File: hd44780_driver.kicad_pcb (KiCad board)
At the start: 2 copper layers, 25 parts, among them J2 BL, J3 Conn_01x08, Q1 2N7002, U1 PCA9555APW

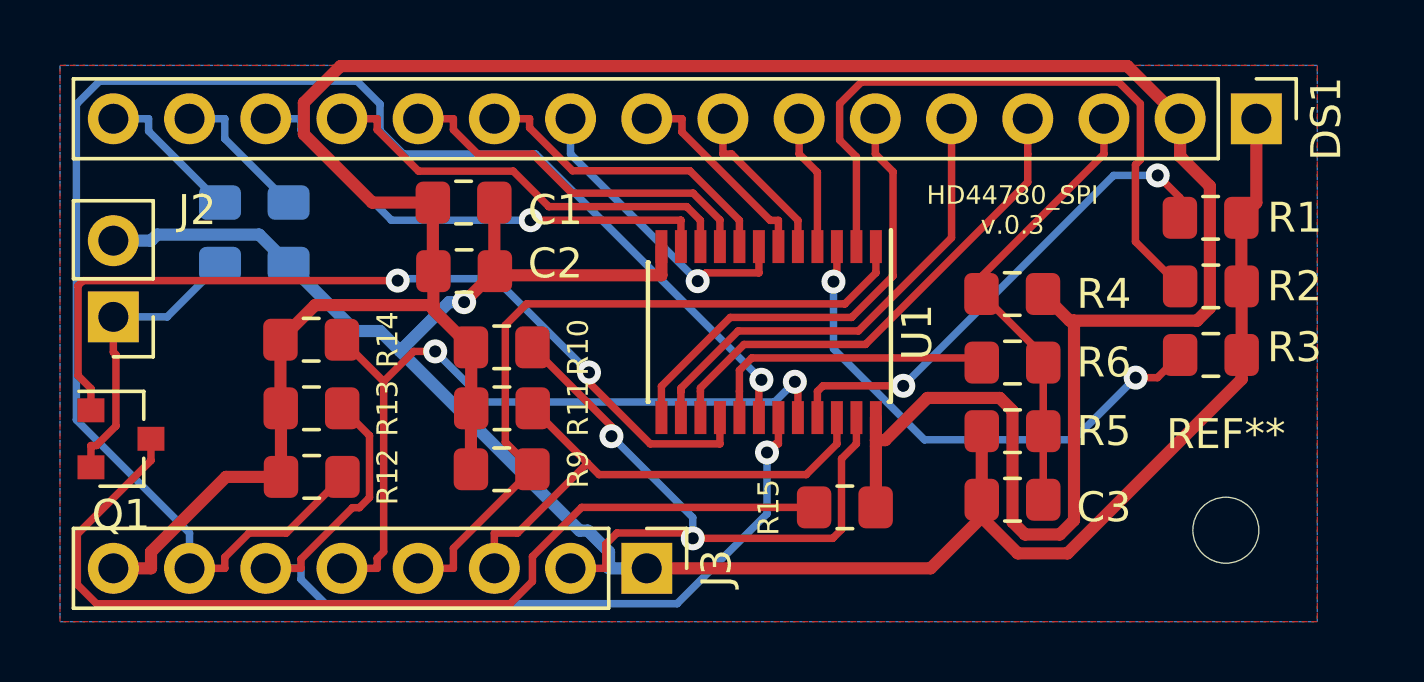
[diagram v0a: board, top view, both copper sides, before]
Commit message: add a input and move VE from the expander to the connector
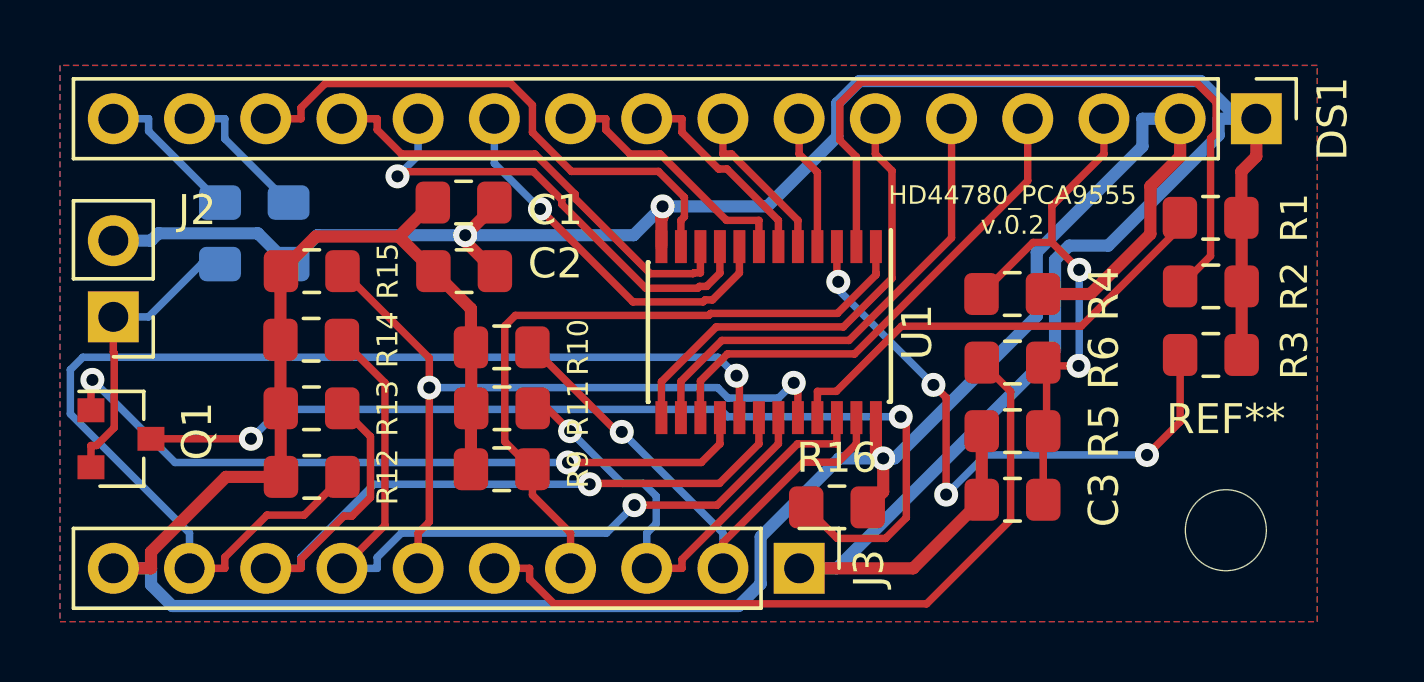
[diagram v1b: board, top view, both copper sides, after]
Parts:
- added R16: 330, Resistor_SMD:R_0805_2012Metric_Pad1.15x1.40mm_HandSolder, F.Cu at (117.6, 42.4)
- J3: value Conn_01x08 -> Conn_01x10; footprint Connector_PinHeader_2.54mm:PinHeader_1x08_P2.54mm_Vertical -> Connector_PinHeader_2.54mm:PinHeader_1x10_P2.54mm_Vertical
- R15: value R -> 10k
- REF**: value MountingHole_2.2mm_M2 -> MountingHole_2.7mm; footprint MountingHole:MountingHole_2.2mm_M2 -> MountingHole:MountingHole_2.7mm
- moved R15 19.4 mm to (100.1, 34.5), turned to 180 degrees
- moved J3 5.08 mm to (116.3, 44.5)
- moved G*** 1.78 mm to (123.2, 40.9)
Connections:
- J3 pad 5: /BUT2 -> /VE
- J3 pad 6: /BUT1 -> /BUT3
- J3 pad 7: /BUT0 -> /BUT2
- J3 pad 8: VCC -> /BUT1
- R15 pad 1: Net-(Q1-Pad3) -> /BUT3
- U1 pad 17: /VE -> /BUT0
- U1 pad 18: /BUT0 -> /BUT1
- U1 pad 19: /BUT1 -> /BUT2
- U1 pad 20: /BUT2 -> /BUT3
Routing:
- net /BUT3: track 0.00 -> 25.0 mm, vias 0 -> 2
- net GND: track 71.1 -> 87.1 mm, vias 1 -> 2
- net /VE: track 9.89 -> 24.7 mm
- net /BUT0: track 52.7 -> 38.9 mm
- net VCC: track 97.4 -> 86.6 mm, vias 0 -> 1
- net /SDA: track 22.7 -> 17.6 mm, vias 2 -> 1
- net /BG: track 29.2 -> 24.2 mm
- net Net-(R3-Pad2): track 17.4 -> 20.8 mm, vias 2 -> 4
- net /D5: track 12.6 -> 15.8 mm, vias 0 -> 1
- net Net-(C3-Pad2): track 15.2 -> 18.1 mm, vias 0 -> 2
- net /BUT1: track 30.0 -> 27.3 mm
- net Net-(R2-Pad2): track 22.4 -> 24.7 mm
- net /D4: track 10.6 -> 12.8 mm, vias 0 -> 1
- net /D7: track 16.3 -> 18.5 mm, vias 1 -> 0
- net /INT: track 24.7 -> 23.0 mm
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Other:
- board text added: "HD44780_PCA9555 v.0.2"
- board text added: "VCC BUT0 BUT1 BUT2 BUT3 VE INT SCL SDA GND"
- board text removed: "HD44780_SPI v.0.3"

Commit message: Change the footprint
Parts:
- U1: footprint Package_SO:TSSOP-24_4.4x7.8mm_P0.65mm -> Package_SO:SSOP-24_5.3x8.2mm_P0.65mm
- moved R16 3.31 mm to (120.7, 43.7), turned to 90 degrees
- moved C3 1.02 mm to (124.5, 42.2)
- moved R4 1.02 mm to (124.5, 35.3)
- moved R5 1.02 mm to (124.5, 39.9)
- moved R6 1.02 mm to (124.5, 37.6)
- moved R10 0.51 mm to (105.9, 37.1)
- moved R11 0.51 mm to (105.9, 39.1)
- moved R9 0.51 mm to (105.9, 41.1)
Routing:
- net Net-(Q1-Pad3): track 33.0 -> 76.0 mm, vias 2 -> 0
- net VCC: track 86.6 -> 72.5 mm, vias 1 -> 0
- net Net-(R2-Pad2): track 24.7 -> 13.3 mm
- net GND: track 87.1 -> 98.0 mm, vias 2 -> 0
- net /BUT0: track 38.9 -> 28.3 mm, vias 1 -> 0
- net /INT: track 23.0 -> 31.0 mm, vias 0 -> 2
- net /RS: track 17.0 -> 24.1 mm, vias 0 -> 1
- net Net-(R3-Pad2): track 20.8 -> 14.3 mm, vias 4 -> 0
- net /SCL: track 17.0 -> 22.2 mm
- net /BG: track 24.2 -> 29.4 mm
- net /BUT1: track 27.3 -> 23.0 mm, vias 1 -> 0
- net /SDA: track 17.6 -> 21.6 mm, vias 1 -> 0
- net Net-(C3-Pad2): track 18.1 -> 15.4 mm, vias 2 -> 1
- net /D4: track 12.8 -> 10.5 mm, vias 1 -> 0
- net /D7: track 18.5 -> 16.2 mm
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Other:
- net class pwr: clearance 0.2032 -> 0.19812; trace_width 0.4064 -> 0.254
